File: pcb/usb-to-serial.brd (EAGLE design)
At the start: 50 x 20 mm, 34 parts, among them CON1 MLW10G, IC1 FT231XS, IC2 STMPS2141STR, IC3 CAT6219-330TDGT3, J1 MINI B, J2 MICRO B, J3 EXT

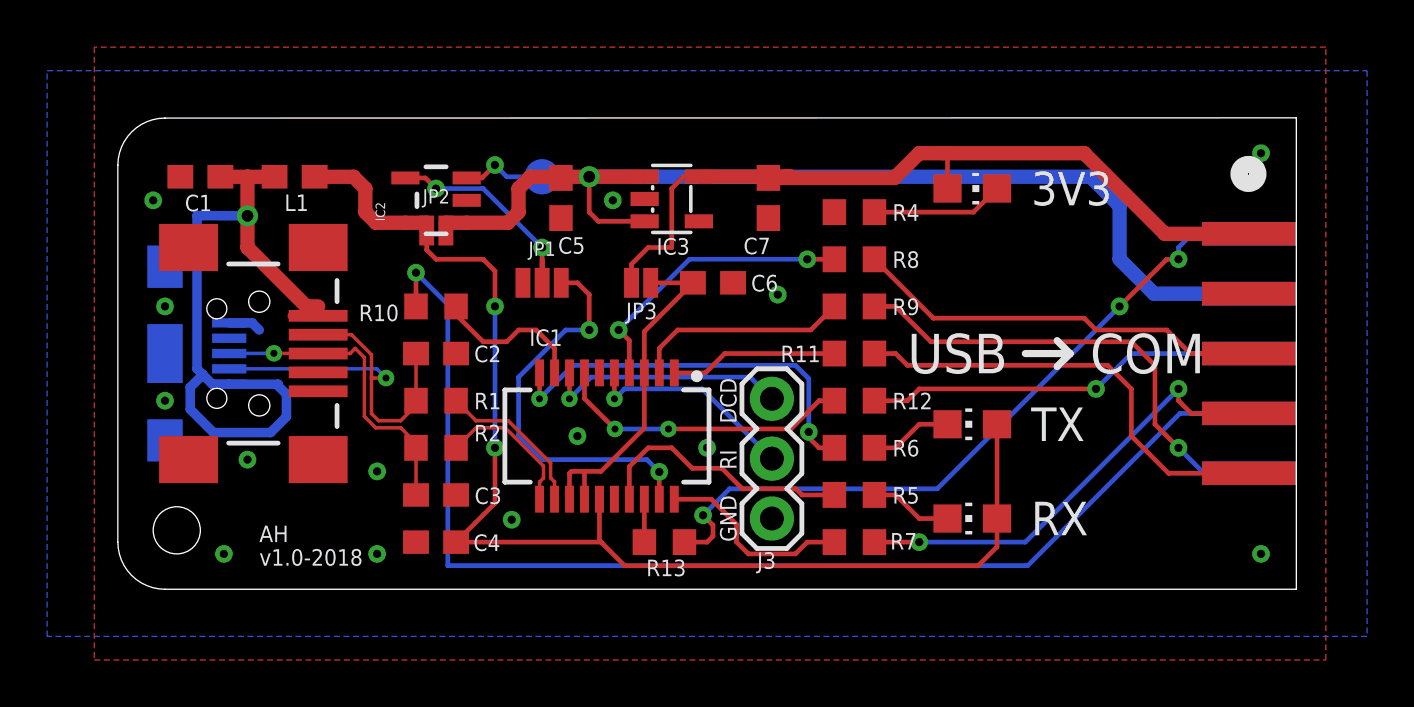
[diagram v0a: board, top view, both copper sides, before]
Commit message: Dev v2 merge to master (#1)
* Update to v2

Changes from Issues:
- Pinout on top/bottom silkscreen
- Add indication LED to error output of IC2 (over current shutdown)
- Add EN pin of IC2 to EXT connector
- Add OSHW logo to silkscreen
Replace mini USB connector with USB-C
- Replace IC3 with XC6210

* Polishing of v2 according to notes from Adam, added schematic in PDF, gerber ZIP package.

* Update of BOM for v2 with Farnell links and prices

* 3D models added, update of Readme and kit manual for v2.

* Update of documentation pictures, readme
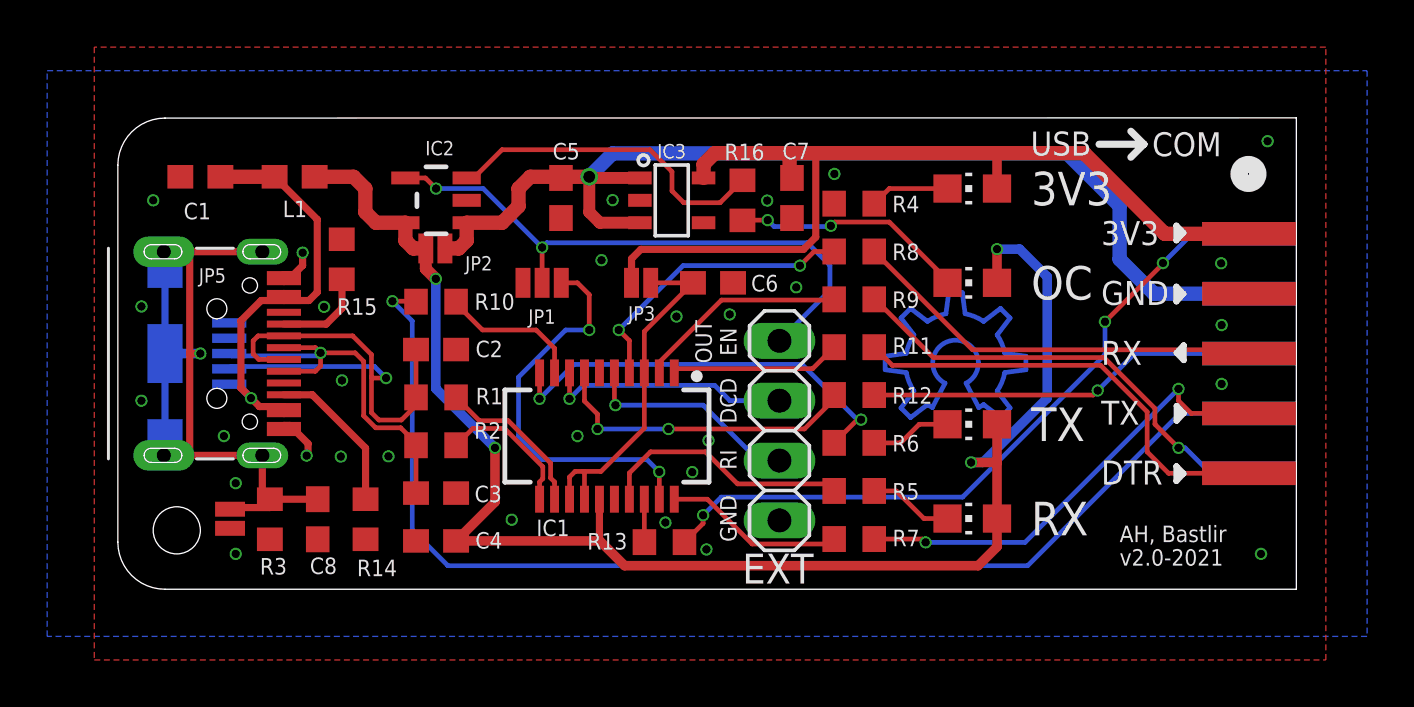
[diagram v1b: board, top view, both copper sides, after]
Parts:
- removed J3: EXT, SparkFun-Connectors:1X03
- removed TP1: TEST_POINT-1.5, testpoints:TP_1.5MM
- added C8: 100nF, rcl:C0603
- added D1: (no value), led:CHIP-LED0805
- added EXT: J3, pinhead:1X04
- added JP5: JUMPER-SMT_2_NO_NO-SILK, SparkFun-Jumpers:SMT-JUMPER_2_NO_NO-SILK
- added R14, R15: 5k1, rcl:R0603
- added R16: 270, rcl:R0603
- added R3: 0, rcl:R0603
- C7: value 2.2uF -> 1uF
- IC3: value CAT6219-330TDGT3 -> XC6210B332MR; device ic-power:TSOT23-5L -> Bastlir:SOT-23-5
- J1: value MINI B -> HRO_31_M_12_USB_C; device SparkFun-Connectors:USB-MINIB -> Bastlir:HRO_31_M_12_USB_C
- moved J1 3.00 mm to (3.00, 10.0), turned to 270 degrees
- moved C7 1.00 mm to (28.6, 16.6)
- moved JP2 0.76 mm to (13.5, 14.5)
- moved R4 0.36 mm to (31.2, 16.4)
- moved R8 0.33 mm to (31.2, 14.3)
- moved R9 0.30 mm to (31.2, 12.3)
- moved R11 0.27 mm to (31.2, 10.3)
- moved R12 0.24 mm to (31.2, 8.24)
- moved R6 0.21 mm to (31.2, 6.21)
- moved R10 0.20 mm to (13.5, 12.2)
- moved R5 0.17 mm to (31.2, 4.17)
- moved C2 0.17 mm to (13.5, 10.2)
- moved R1 0.14 mm to (13.5, 8.14)
- moved R7 0.13 mm to (31.2, 2.13)
- moved R2 0.11 mm to (13.5, 6.11)
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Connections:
- removed net N$4: C1.1, J1.VBUS, J2.VBUS, L1.2
- removed net N$6: IC2.3, TP1.TP
- new net N$11: D1.C, R16.2
- new net N$7: J1.B5, R14.2
- new net N$8: C8.1, J1.S1, J1.S2, J1.S3, J1.S4, J2.SHIELD1, J2.SHIELD2, J2.SHIELD3, JP5.2, R3.2
- new net OC_ERR: IC2.3, R16.1
- new net OUT_EN: EXT.4, IC2.4, JP1.2
- new net VBUS: C1.1, J1.A4, J1.A9, J1.B4, J1.B9, J2.VBUS, L1.2
- net +5V: now also D1.A
- net DCD: now also EXT.3; no longer J3.3
- net GND: now also C8.2, EXT.1, J1.A1, J1.A12, J1.B1, J1.B12, JP5.1, R14.1, R15.1, R3.1; no longer J1.GND, J1.S1, J1.S2, J1.S3, J1.S4, J2.SHIELD1, J2.SHIELD2, J2.SHIELD3, J3.1
- net N$2: now also J1.A5, R15.2; no longer IC2.4, JP1.2
- net RI: now also EXT.2; no longer J3.2
- net USBD_N: now also J1.A7, J1.B7; no longer J1.D-
- net USBD_P: now also J1.A6, J1.B6; no longer J1.D+
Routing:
- net N$8: track 0.00 -> 32.4 mm, vias 0 -> 1
- net OUT_EN: track 0.00 -> 25.3 mm, vias 0 -> 2
- net VBUS: track 0.00 -> 18.5 mm, vias 0 -> 1
- net OC_ERR: track 0.00 -> 14.0 mm
- net +5V: track 54.0 -> 66.7 mm, vias 2 -> 4
- net N$11: track 0.00 -> 10.0 mm, vias 0 -> 2
- net N$7: track 0.00 -> 6.57 mm
- net N$2: track 9.52 -> 3.98 mm, vias 2 -> 0
- net 3V3_OUT: track 35.3 -> 40.7 mm
- net USBD_N: track 17.0 -> 22.0 mm
- net N$4: track 31.2 -> 27.2 mm, vias 1 -> 0
- net N$6: track 3.63 -> 0.00 mm, vias 1 -> 0
- net USBD_P: track 13.3 -> 16.9 mm
- net GND: track 1.40 -> 3.98 mm, vias 14 -> 30
- net CTS: track 52.4 -> 49.9 mm
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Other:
- board text added: "3V3 GND RX TX DTR"
- board text added: "AH, Bastlir"
- board text added: "OC"
- board text added: "OUT EN"
- board text added: "TXDEN 5V_OUT DSR CTS RTS"
- board text added: "v2.0-2021"
- board text removed: "AH"
- board text removed: "v1.0-2018"
